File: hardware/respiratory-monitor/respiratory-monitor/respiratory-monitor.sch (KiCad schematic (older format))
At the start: 6 parts

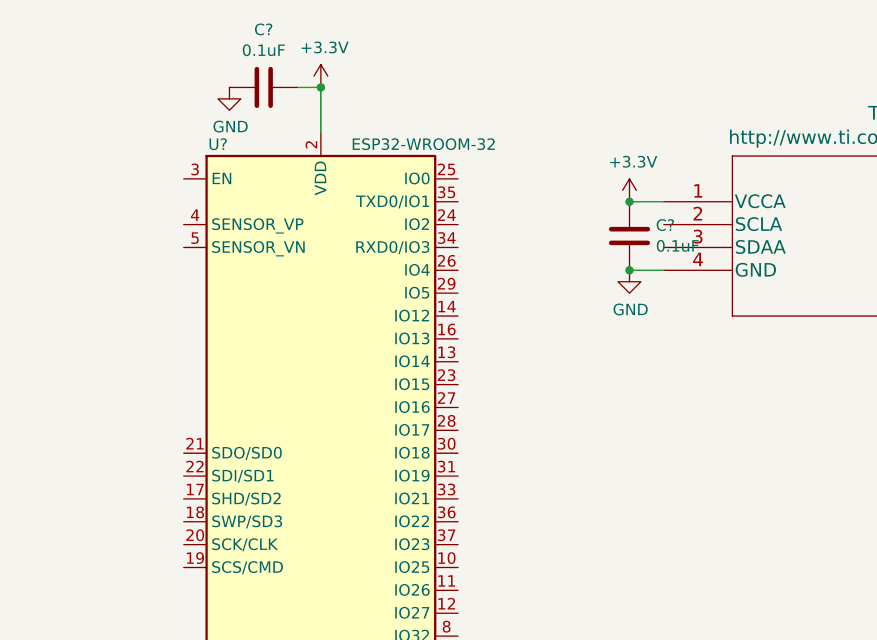
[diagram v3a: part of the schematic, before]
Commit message: Set the I2C pins to the ESP32 device
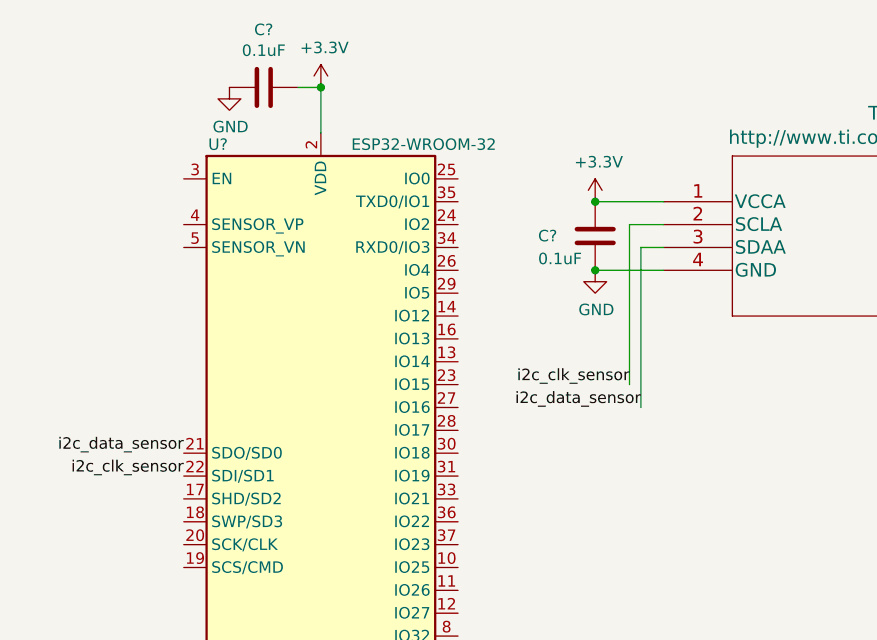
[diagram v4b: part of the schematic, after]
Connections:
- net i2c_data_sensor: now reaches U?.21 (SDO/SD0)
- net i2c_data_sensor: now also U?.3 (SDAA)
- net i2c_clk_sensor: now reaches U?.22 (SDI/SD1)
- net i2c_clk_sensor: now also U?.2 (SCLA)
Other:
- moved on the sheet: C?
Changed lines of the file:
@@
 $EndComp
+$Comp
+L power:GND #PWR?
+U 1 1 5E951891
+P 1750 3850
+F 0 "#PWR?" H 1750 3600 50  0001 C CNN
+F 1 "GND" H 1755 3677 50  0000 C CNN
+F 2 "" H 1750 3850 50  0001 C CNN
+F 3 "" H 1750 3850 50  0001 C CNN
+	1    1750 3850
+	1    0    0    -1
+$EndComp
+$Comp
+L power:GND #PWR?
+U 1 1 5E955F09
+P 2950 1650
+F 0 "#PWR?" H 2950 1400 50  0001 C CNN
+F 1 "GND" H 2955 1477 50  0000 C CNN
+F 2 "" H 2950 1650 50  0001 C CNN
+F 3 "" H 2950 1650 50  0001 C CNN
+	1    2950 1650
+	1    0    0    -1
+$EndComp
+$Comp
+L power:GND #PWR?
+U 1 1 5E958A2D
+P 6650 1950
+F 0 "#PWR?" H 6650 1700 50  0001 C CNN
+F 1 "GND" V 6655 1822 50  0000 R CNN
+F 2 "" H 6650 1950 50  0001 C CNN
+F 3 "" H 6650 1950 50  0001 C CNN
+	1    6650 1950
+	-1   0    0    1
+$EndComp
+$Comp
+L power:+5V #PWR?
+U 1 1 5E95987C
+P 6450 1950
+F 0 "#PWR?" H 6450 1800 50  0001 C CNN
+F 1 "+5V" V 6465 2078 50  0000 L CNN
+F 2 "" H 6450 1950 50  0001 C CNN
+F 3 "" H 6450 1950 50  0001 C CNN
+	1    6450 1950
+	1    0    0    -1
+$EndComp
+$Comp
+L power:+5V #PWR?
+U 1 1 5E95A00A
+P 6850 1950
+F 0 "#PWR?" H 6850 1800 50  0001 C CNN
+F 1 "+5V" V 6865 2078 50  0000 L CNN
+F 2 "" H 6850 1950 50  0001 C CNN
+F 3 "" H 6850 1950 50  0001 C CNN
+	1    6850 1950
+	1    0    0    -1
+$EndComp
+$Comp
+L power:GND #PWR?
+U 1 1 5E95A62D
+P 6350 1950
+F 0 "#PWR?" H 6350 1700 50  0001 C CNN
+F 1 "GND" V 6355 1822 50  0000 R CNN
+F 2 "" H 6350 1950 50  0001 C CNN
+F 3 "" H 6350 1950 50  0001 C CNN
+	1    6350 1950
+	-1   0    0    1
+$EndComp
+$Comp
+L power:+5V #PWR?
+U 1 1 5E95A820
+P 5750 1950
+F 0 "#PWR?" H 5750 1800 50  0001 C CNN
+F 1 "+5V" V 5765 2078 50  0000 L CNN
+F 2 "" H 5750 1950 50  0001 C CNN
+F 3 "" H 5750 1950 50  0001 C CNN
+	1    5750 1950
+	0    1    1    0
+$EndComp
+$Comp
+L Connector:Conn_01x06_Male J?
+U 1 1 5E94E61D
+P 6550 2150
+F 0 "J?" H 6850 2450 50  0000 C CNN
+F 1 "SFM3xxx_Conn_06_Male" H 6300 2450 50  0000 C CNN
+F 2 "" H 6550 2150 50  0001 C CNN
+F 3 "https://media.digikey.com/pdf/Data%20Sheets/Sensirion%20PDFs/Sensirion_Mass_Flow_Meters_SFM3300_Datasheet.pdf" H 6550 2150 50  0001 C CNN
+	1    6550 2150
+	0    -1   -1   0
+$EndComp
+$Comp
+L Device:C C?
+U 1 1 5E96635E
+P 2950 1500
+F 0 "C?" H 2700 1500 50  0000 L CNN
+F 1 "0.1uF" H 2700 1400 50  0000 L CNN
+F 2 "" H 2988 1350 50  0001 C CNN
+F 3 "~" H 2950 1500 50  0001 C CNN
+	1    2950 1500
+	1    0    0    -1
+$EndComp
+$Comp
+L Device:C C?
+U 1 1 5E966B53
+P 5750 2100
+F 0 "C?" H 5865 2146 50  0000 L CNN
+F 1 "0.1uF" H 5865 2055 50  0000 L CNN
+F 2 "" H 5788 1950 50  0001 C CNN
+F 3 "~" H 5750 2100 50  0001 C CNN
+	1    5750 2100
+	1    0    0    -1
+$EndComp
+$Comp
+L power:GND #PWR?
+U 1 1 5E9671DA
+P 5750 2250
+F 0 "#PWR?" H 5750 2000 50  0001 C CNN
+F 1 "GND" H 5755 2077 50  0000 C CNN
+F 2 "" H 5750 2250 50  0001 C CNN
+F 3 "" H 5750 2250 50  0001 C CNN
+	1    5750 2250
+	1    0    0    -1
+$EndComp
+Wire Wire Line
+	5750 1950 5750 1350
+Connection ~ 5750 1950
+Wire Wire Line
+	6550 1950 6550 1450
+Wire Wire Line
+	6750 1550 6750 1950
+$Comp
+L power:GND #PWR?
+U 1 1 5E972038
+P 1350 850
+F 0 "#PWR?" H 1350 600 50  0001 C CNN
+F 1 "GND" H 1355 677 50  0000 C CNN
+F 2 "" H 1350 850 50  0001 C CNN
+F 3 "" H 1350 850 50  0001 C CNN
+	1    1350 850
+	1    0    0    -1
+$EndComp
+$Comp
+L Device:C C?
+U 1 1 5E9726C9
+P 1500 850
+F 0 "C?" V 1248 850 50  0000 C CNN
+F 1 "0.1uF" V 1339 850 50  0000 C CNN
+F 2 "" H 1538 700 50  0001 C CNN
+F 3 "~" H 1500 850 50  0001 C CNN
+	1    1500 850
+	0    1    1    0
+$EndComp
+Wire Wire Line
+	1750 850  1750 1050
+$Comp
+L power:+3.3V #PWR?
+U 1 1 5E973DA6
+P 1750 850
+F 0 "#PWR?" H 1750 700 50  0001 C CNN
+F 1 "+3.3V" H 1765 1023 50  0000 C CNN
+F 2 "" H 1750 850 50  0001 C CNN
+F 3 "" H 1750 850 50  0001 C CNN
+	1    1750 850
+	1    0    0    -1
+$EndComp
+$Comp
+L power:+3.3V #PWR?
+U 1 1 5E97487C
+P 2950 1350
+F 0 "#PWR?" H 2950 1200 50  0001 C CNN
+F 1 "+3.3V" H 2965 1523 50  0000 C CNN
+F 2 "" H 2950 1350 50  0001 C CNN
+F 3 "" H 2950 1350 50  0001 C CNN
+	1    2950 1350
+	1    0    0    -1
+$EndComp
+Connection ~ 2950 1350
+Wire Wire Line
+	1650 850  1750 850
+Connection ~ 1750 850
+Text Label 1150 2450 2    50   ~ 0
+i2c_data_sensor
+Text Label 1150 2550 2    50   ~ 0
+i2c_clk_sensor
+Text Label 3150 2250 2    50   ~ 0
+i2c_data_sensor
+Text Label 3100 2150 2    50   ~ 0
+i2c_clk_sensor
+Wire Wire Line
+	5750 1350 5650 1350
+Wire Wire Line
+	6550 1450 5650 1450
+Wire Wire Line
+	5650 1550 6750 1550
+Wire Wire Line
+	3250 1350 2950 1350
 $Comp
 L proj-components:TCA9509DGKR U?
@@
 	1    0    0    -1
 $EndComp
-$Comp
-L power:GND #PWR?
-U 1 1 5E951891
-P 1750 3850
-F 0 "#PWR?" H 1750 3600 50  0001 C CNN
-F 1 "GND" H 1755 3677 50  0000 C CNN
-F 2 "" H 1750 3850 50  0001 C CNN
-F 3 "" H 1750 3850 50  0001 C CNN
-	1    1750 3850
-	1    0    0    -1
-$EndComp
-$Comp
-L power:GND #PWR?
-U 1 1 5E955F09
-P 3100 1650
-F 0 "#PWR?" H 3100 1400 50  0001 C CNN
-F 1 "GND" H 3105 1477 50  0000 C CNN
-F 2 "" H 3100 1650 50  0001 C CNN
-F 3 "" H 3100 1650 50  0001 C CNN
-	1    3100 1650
-	1    0    0    -1
-$EndComp
-$Comp
-L power:GND #PWR?
-U 1 1 5E958A2D
-P 6650 1950
-F 0 "#PWR?" H 6650 1700 50  0001 C CNN
-F 1 "GND" V 6655 1822 50  0000 R CNN
-F 2 "" H 6650 1950 50  0001 C CNN
-F 3 "" H 6650 1950 50  0001 C CNN
-	1    6650 1950
-	-1   0    0    1
-$EndComp
-$Comp
-L power:+5V #PWR?
-U 1 1 5E95987C
-P 6450 1950
-F 0 "#PWR?" H 6450 1800 50  0001 C CNN
-F 1 "+5V" V 6465 2078 50  0000 L CNN
-F 2 "" H 6450 1950 50  0001 C CNN
-F 3 "" H 6450 1950 50  0001 C CNN
-	1    6450 1950
-	1    0    0    -1
-$EndComp
-$Comp
-L power:+5V #PWR?
-U 1 1 5E95A00A
-P 6850 1950
-F 0 "#PWR?" H 6850 1800 50  0001 C CNN
-F 1 "+5V" V 6865 2078 50  0000 L CNN
-F 2 "" H 6850 1950 50  0001 C CNN
-F 3 "" H 6850 1950 50  0001 C CNN
-	1    6850 1950
-	1    0    0    -1
-$EndComp
-$Comp
-L power:GND #PWR?
-U 1 1 5E95A62D
-P 6350 1950
-F 0 "#PWR?" H 6350 1700 50  0001 C CNN
-F 1 "GND" V 6355 1822 50  0000 R CNN
-F 2 "" H 6350 1950 50  0001 C CNN
-F 3 "" H 6350 1950 50  0001 C CNN
-	1    6350 1950
-	-1   0    0    1
-$EndComp
-$Comp
-L power:+5V #PWR?
-U 1 1 5E95A820
-P 5750 1950
-F 0 "#PWR?" H 5750 1800 50  0001 C CNN
-F 1 "+5V" V 5765 2078 50  0000 L CNN
-F 2 "" H 5750 1950 50  0001 C CNN
-F 3 "" H 5750 1950 50  0001 C CNN
-	1    5750 1950
-	0    1    1    0
-$EndComp
-$Comp
-L Connector:Conn_01x06_Male J?
-U 1 1 5E94E61D
-P 6550 2150
-F 0 "J?" H 6850 2450 50  0000 C CNN
-F 1 "SFM3xxx_Conn_06_Male" H 6300 2450 50  0000 C CNN
-F 2 "" H 6550 2150 50  0001 C CNN
-F 3 "https://media.digikey.com/pdf/Data%20Sheets/Sensirion%20PDFs/Sensirion_Mass_Flow_Meters_SFM3300_Datasheet.pdf" H 6550 2150 50  0001 C CNN
-	1    6550 2150
-	0    -1   -1   0
-$EndComp
-Wire Wire Line
-	3100 1650 3250 1650
-Wire Wire Line
-	3250 1350 3100 1350
-$Comp
-L Device:C C?
-U 1 1 5E96635E
-P 3100 1500
-F 0 "C?" H 3215 1546 50  0000 L CNN
-F 1 "0.1uF" H 3215 1455 50  0000 L CNN
-F 2 "" H 3138 1350 50  0001 C CNN
-F 3 "~" H 3100 1500 50  0001 C CNN
-	1    3100 1500
-	1    0    0    -1
-$EndComp
-Connection ~ 3100 1650
-$Comp
-L Device:C C?
-U 1 1 5E966B53
-P 5750 2100
-F 0 "C?" H 5865 2146 50  0000 L CNN
-F 1 "0.1uF" H 5865 2055 50  0000 L CNN
-F 2 "" H 5788 1950 50  0001 C CNN
-F 3 "~" H 5750 2100 50  0001 C CNN
-	1    5750 2100
-	1    0    0    -1
-$EndComp
-$Comp
-L power:GND #PWR?
-U 1 1 5E9671DA
-P 5750 2250
-F 0 "#PWR?" H 5750 2000 50  0001 C CNN
-F 1 "GND" H 5755 2077 50  0000 C CNN
-F 2 "" H 5750 2250 50  0001 C CNN
-F 3 "" H 5750 2250 50  0001 C CNN
-	1    5750 2250
-	1    0    0    -1
-$EndComp
-Wire Wire Line
-	5750 1950 5750 1350
-Wire Wire Line
-	5750 1350 5650 1350
-Connection ~ 5750 1950
-Wire Wire Line
-	6550 1950 6550 1450
-Wire Wire Line
-	6550 1450 5650 1450
-Wire Wire Line
-	5650 1550 6750 1550
-Wire Wire Line
-	6750 1550 6750 1950
-$Comp
-L power:GND #PWR?
-U 1 1 5E972038
-P 1350 850
-F 0 "#PWR?" H 1350 600 50  0001 C CNN
-F 1 "GND" H 1355 677 50  0000 C CNN
-F 2 "" H 1350 850 50  0001 C CNN
-F 3 "" H 1350 850 50  0001 C CNN
-	1    1350 850
-	1    0    0    -1
-$EndComp
-$Comp
-L Device:C C?
-U 1 1 5E9726C9
-P 1500 850
-F 0 "C?" V 1248 850 50  0000 C CNN
-F 1 "0.1uF" V 1339 850 50  0000 C CNN
-F 2 "" H 1538 700 50  0001 C CNN
-F 3 "~" H 1500 850 50  0001 C CNN
-	1    1500 850
-	0    1    1    0
-$EndComp
-Wire Wire Line
-	1750 850  1750 1050
-$Comp
-L power:+3.3V #PWR?
-U 1 1 5E973DA6
-P 1750 850
-F 0 "#PWR?" H 1750 700 50  0001 C CNN
-F 1 "+3.3V" H 1765 1023 50  0000 C CNN
-F 2 "" H 1750 850 50  0001 C CNN
-F 3 "" H 1750 850 50  0001 C CNN
-	1    1750 850
-	1    0    0    -1
-$EndComp
-$Comp
-L power:+3.3V #PWR?
-U 1 1 5E97487C
-P 3100 1350
-F 0 "#PWR?" H 3100 1200 50  0001 C CNN
-F 1 "+3.3V" H 3115 1523 50  0000 C CNN
-F 2 "" H 3100 1350 50  0001 C CNN
-F 3 "" H 3100 1350 50  0001 C CNN
-	1    3100 1350
-	1    0    0    -1
-$EndComp
-Connection ~ 3100 1350
-Wire Wire Line
-	1650 850  1750 850
-Connection ~ 1750 850
+Wire Wire Line
+	3100 1450 3250 1450
+Wire Wire Line
+	3150 2250 3150 1550
+Wire Wire Line
+	3150 1550 3250 1550
+Wire Wire Line
+	3100 1450 3100 2150
+Wire Wire Line
+	2950 1650 3250 1650
+Connection ~ 2950 1650
 $EndSCHEMATC
